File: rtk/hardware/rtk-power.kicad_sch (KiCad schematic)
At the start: 7 parts

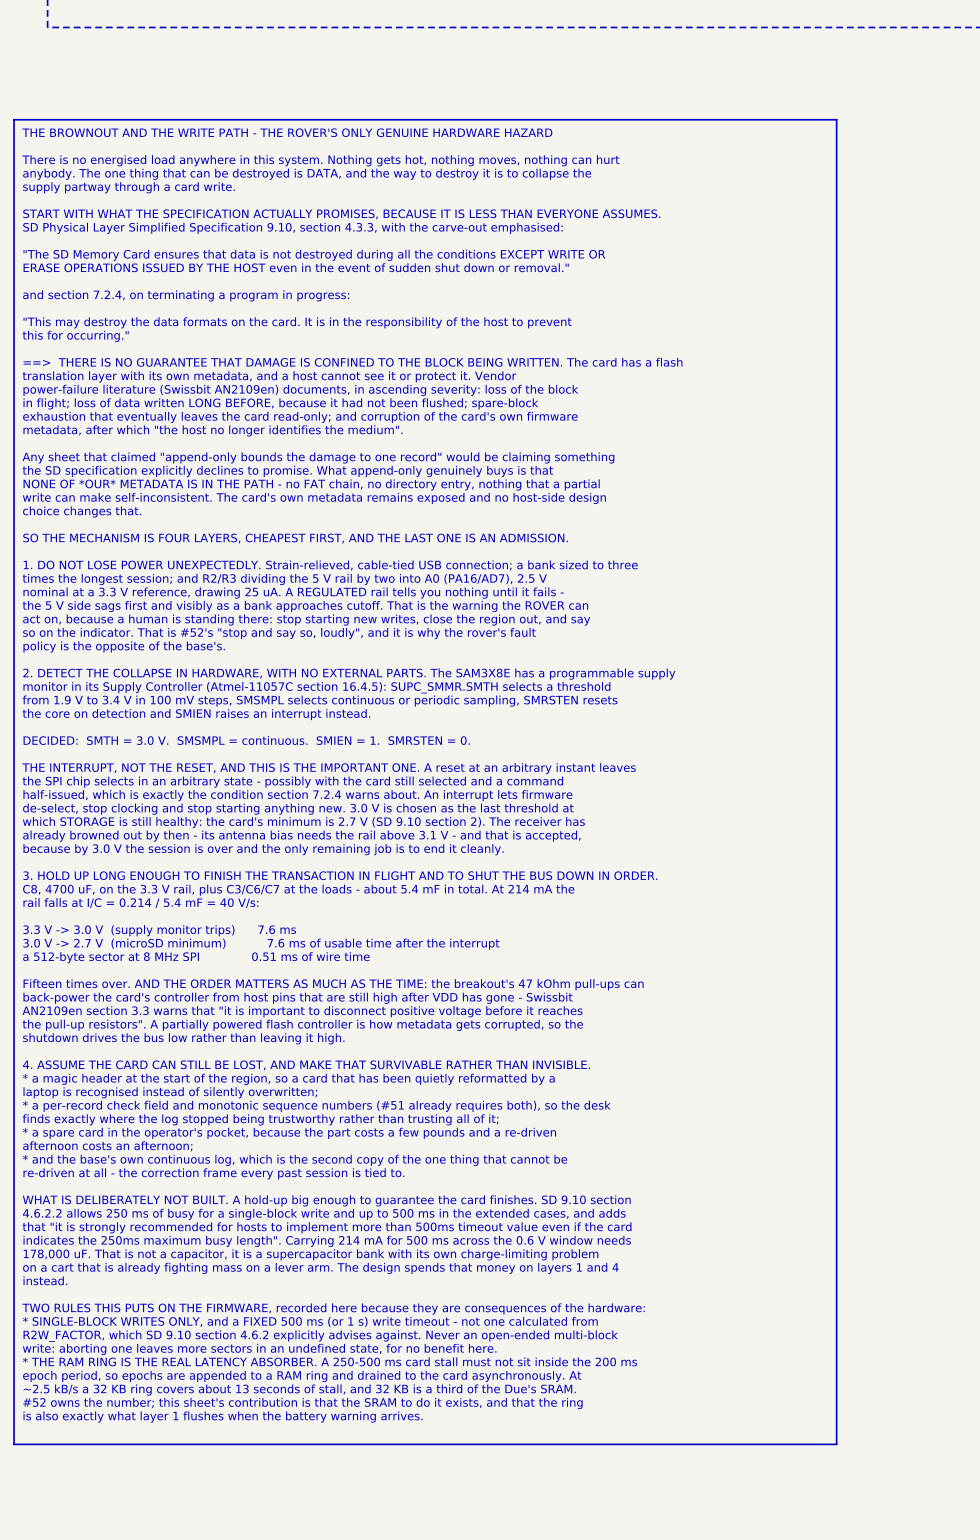
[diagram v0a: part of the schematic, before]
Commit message: fix(rtk): correct the microSD citations after verifying them against the spec
The subagent that researched the SD-card facts retracted them as fabricated
after I had already committed. I re-verified every one against documents I
downloaded and read myself: the Physical Layer Simplified Specification 3.01
(and 9.10 for the current numbering), Swissbit AN2109en, and Adafruit's
schematic and guide.

Most of it held. The quotations in section 4.3.3 ("except write or erase
operations issued by the host"), section 7.2.4 ("may destroy the data formats
on the card"), the 250 ms busy limit, the fixed-timeout application notes, the
2.7-3.6 V range and the 100 mA SPI-mode ceiling are all verbatim and correctly
attributed. Three things were not:

  * The card-detect pin is DET, not CARDDET, and its pull-up is a value the
    vendor contradicts itself on — 4.7 k in the guide, 47 k in the shipped
    schematic. The sheet now names the pin correctly and records the
    disagreement rather than picking one silently. Nothing depends on which:
    70 uA into a pin whose leakage is 18 nA, on a pin that keeps its
    hysteresis.
  * The 500 ms busy allowance is specific to SDXC/SDUC in four enumerated
    cases, not a general extension of the 250 ms limit.
  * The "use a fixed timeout, not R2W_FACTOR" advice is section 4.6.2's
    application notes, not 4.6.2.2.

Also added, because it follows from 7.2.4 and was missing: never CMD0 a busy
card to escape a hung write — that is the exact action the specification warns
destroys on-card data formats. And the 100 mA figure is a one-second average;
no vendor publishes an instantaneous peak, which is the second reason C6 is
generous.

ERC still passes with zero violations at --severity=all.

Co-Authored-By: Claude Opus 5 <noreply@anthropic.com>
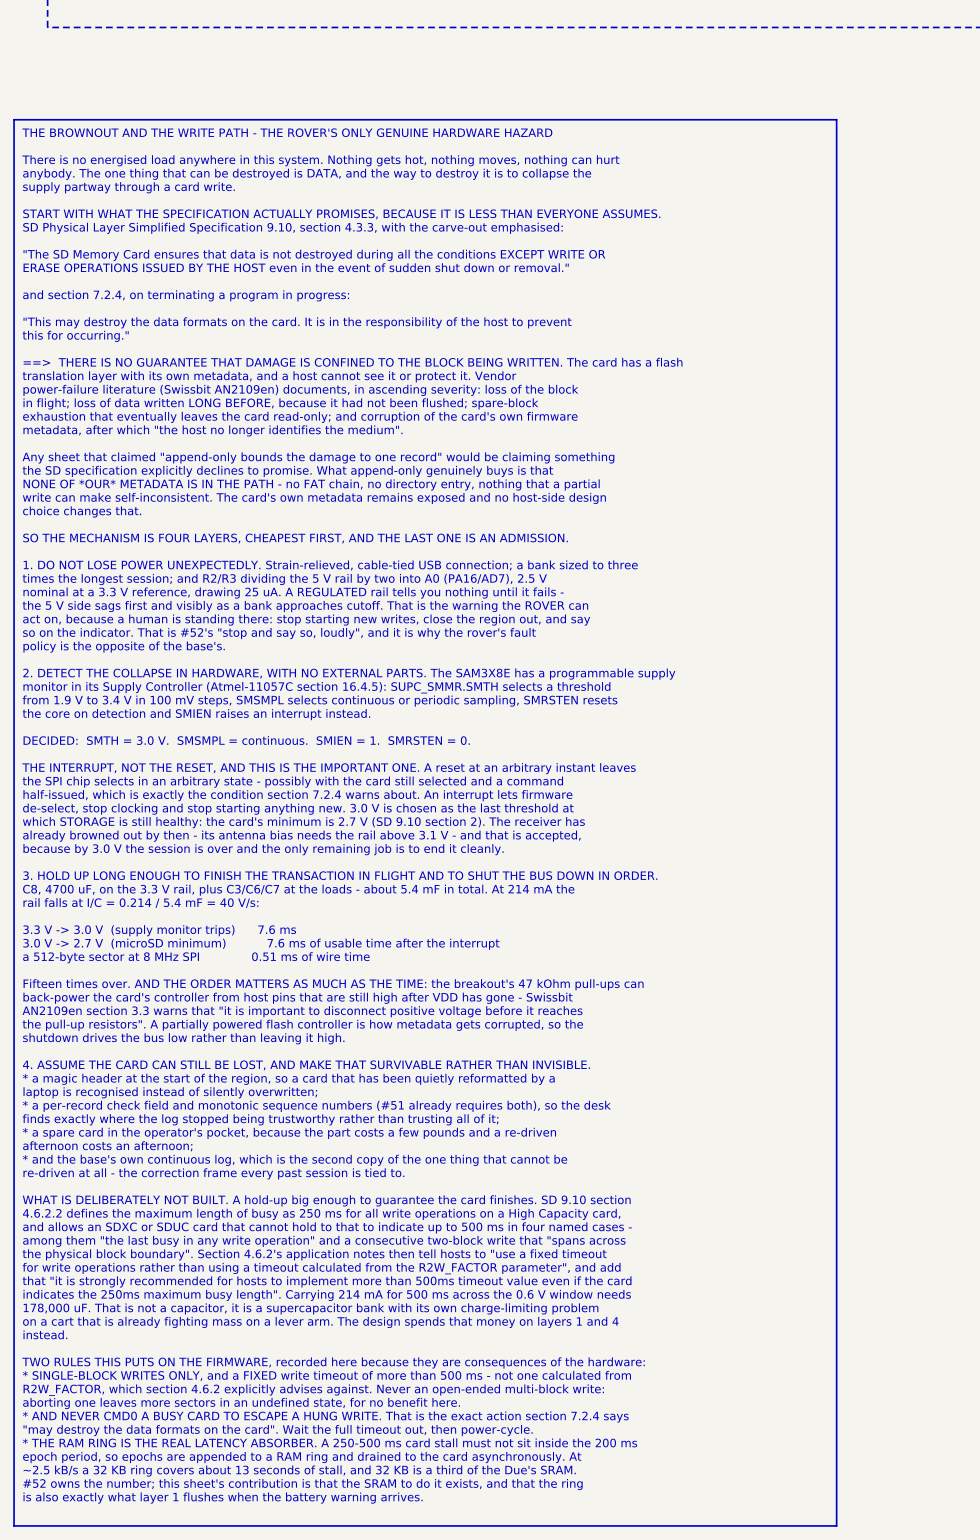
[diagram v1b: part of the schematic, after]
